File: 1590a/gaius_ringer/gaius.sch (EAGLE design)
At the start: 30 parts, among them Q1 2N5088, Q2 2N3906, Q3 2N5088

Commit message: finished chorus and tremolo baords; other tweaks & polish
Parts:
- removed PAD1: PADSQR, supply pins:PADSQR
- removed PAD3: PADRND, supply pins:PADRND
- added 9V: DC_MONO, jacks:DC_MONO
- C1, C3, C4, C5: device capacitors-film:CER/FILMBOX.1 -> capacitors-film:CER/FILM2
- D1: device diodes:DO41.2 -> diodes:DO41.3
- renumbered PAD2 to IN, PAD4 to GND, PAD5 to OUT
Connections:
- net IN1 renamed IN
- net OUT1 renamed OUT
- removed net +9V: D1.A, PAD1.P$1
- new net N$13: 9V.TIP, D1.A
- net GND: no longer PAD3.P$1
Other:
- note added: "OCTAVER / RING MODULATOR based on the dan armstrong green ringer (c)2016 burr settles"
- note removed: "OCTAVER / RING MODULATOR based on the dan armstrong green ringer (c) 2016 burr settles"
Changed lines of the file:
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@@
 <drawing>
 <settings>
-<setting alwaysvectorfont="no"/>
+<setting alwaysvectorfont="yes"/>
 <setting verticaltext="up"/>
 </settings>
@@
 </classes>
 <parts>
-<part name="C1" library="capacitors-film" deviceset="CER/FILM" device="BOX.1" value="47n"/>
+<part name="C1" library="capacitors-film" deviceset="CER/FILM" device="2" value="47n"/>
 <part name="R3" library="resistors" deviceset="R_" device=".3B" value="160k"/>
 <part name="R2" library="resistors" deviceset="R_" device=".3B" value="470k"/>
@@
 <part name="R7" library="resistors" deviceset="R_" device=".3B" value="10k"/>
 <part name="GND5" library="supply pins" deviceset="GND" device=""/>
-<part name="C3" library="capacitors-film" deviceset="CER/FILM" device="BOX.1" value="47n"/>
+<part name="C3" library="capacitors-film" deviceset="CER/FILM" device="2" value="47n"/>
 <part name="NULL" library="potentiometers" deviceset="POTS" device="TRIM" value="25kB"/>
-<part name="C4" library="capacitors-film" deviceset="CER/FILM" device="BOX.1" value="47n"/>
+<part name="C4" library="capacitors-film" deviceset="CER/FILM" device="2" value="47n"/>
 <part name="R9" library="resistors" deviceset="R_" device=".3B" value="68k"/>
 <part name="R8" library="resistors" deviceset="R_" device=".3B" value="68k"/>
@@
 <part name="R13" library="resistors" deviceset="R_" device=".3B" value="47k"/>
 <part name="GND8" library="supply pins" deviceset="GND" device=""/>
-<part name="D1" library="diodes" deviceset="DO41" device=".2" value="1N5817"/>
+<part name="D1" library="diodes" deviceset="DO41" device=".3" value="1N5817"/>
 <part name="C2" library="capacitors-elec" deviceset="050" device="1" value="100u"/>
 <part name="GND2" library="supply pins" deviceset="GND" device=""/>
-<part name="V1" library="gm-supply" deviceset="+9V" device=""/>
-<part name="IN1" library="gm-supply" deviceset="IN" device=""/>
-<part name="OUT1" library="gm-supply" deviceset="OUT" device=""/>
 <part name="GND1" library="supply pins" deviceset="GND" device=""/>
-<part name="PAD1" library="supply pins" deviceset="PAD" device="SQR"/>
-<part name="PAD2" library="supply pins" deviceset="PAD" device="SQR"/>
-<part name="PAD5" library="supply pins" deviceset="PAD" device="SQR"/>
-<part name="PAD3" library="supply pins" deviceset="PAD" device="RND"/>
-<part name="PAD4" library="supply pins" deviceset="PAD" device="RND"/>
-<part name="C5" library="capacitors-film" deviceset="CER/FILM" device="BOX.1" value="100n"/>
+<part name="IN" library="supply pins" deviceset="PAD" device="SQR"/>
+<part name="OUT" library="supply pins" deviceset="PAD" device="SQR"/>
+<part name="GND" library="supply pins" deviceset="PAD" device="RND"/>
+<part name="C5" library="capacitors-film" deviceset="CER/FILM" device="2" value="100n"/>
+<part name="9V" library="jacks" deviceset="DC_MONO" device=""/>
 </parts>
 <sheets>
@@
 <text x="2.54" y="2.54" size="1.9304" layer="97">OCTAVER / RING MODULATOR
 based on the dan armstrong green ringer
-(c) 2016 burr settles</text>
+(c)2016 burr settles</text>
 </plain>
 <instances>
@@
 <instance part="D1" gate="G$1" x="17.78" y="88.9"/>
 <instance part="C2" gate="1" x="27.94" y="78.74" rot="MR270"/>
-<instance part="GND2" gate="GND" x="27.94" y="66.04"/>
-<instance part="V1" gate="+9V" x="5.08" y="88.9" rot="R90"/>
-<instance part="IN1" gate="G$1" x="5.08" y="48.26"/>
-<instance part="OUT1" gate="G$1" x="132.08" y="43.18"/>
+<instance part="GND2" gate="GND" x="27.94" y="68.58"/>
 <instance part="GND1" gate="GND" x="17.78" y="27.94"/>
-<instance part="PAD1" gate="G$1" x="7.62" y="88.9"/>
-<instance part="PAD2" gate="G$1" x="7.62" y="48.26"/>
-<instance part="PAD5" gate="G$1" x="129.54" y="43.18"/>
-<instance part="PAD3" gate="G$1" x="27.94" y="68.58" rot="R90"/>
-<instance part="PAD4" gate="G$1" x="121.92" y="30.48" rot="R90"/>
+<instance part="IN" gate="G$1" x="7.62" y="48.26"/>
+<instance part="OUT" gate="G$1" x="129.54" y="43.18"/>
+<instance part="GND" gate="G$1" x="121.92" y="30.48" rot="R90"/>
 <instance part="C5" gate="G$1" x="114.3" y="43.18"/>
+<instance part="9V" gate="DC" x="5.08" y="86.36"/>
 </instances>
 <busses>
@@
 <pinref part="R13" gate="G$1" pin="1"/>
 <pinref part="GND8" gate="GND" pin="GND"/>
-<pinref part="PAD4" gate="G$1" pin="P$1"/>
+<pinref part="GND" gate="G$1" pin="P$1"/>
 <junction x="121.92" y="30.48"/>
-<pinref part="PAD4" gate="G$1" pin="P$1"/>
+<pinref part="GND" gate="G$1" pin="P$1"/>
 </segment>
 <segment>
@@
 <pinref part="C2" gate="1" pin="-"/>
 <pinref part="GND2" gate="GND" pin="GND"/>
-<wire x1="27.94" y1="73.66" x2="27.94" y2="68.58" width="0.1524" layer="91"/>
-<pinref part="PAD3" gate="G$1" pin="P$1"/>
-<pinref part="PAD3" gate="G$1" pin="P$1"/>
-<junction x="27.94" y="68.58"/>
+<wire x1="27.94" y1="73.66" x2="27.94" y2="71.12" width="0.1524" layer="91"/>
 </segment>
 </net>
@@
 </segment>
 </net>
-<net name="+9V" class="0">
-<segment>
-<pinref part="V1" gate="+9V" pin="+9V"/>
-<pinref part="PAD1" gate="G$1" pin="P$1"/>
-<pinref part="D1" gate="G$1" pin="A"/>
-<wire x1="12.7" y1="88.9" x2="7.62" y2="88.9" width="0.1524" layer="91"/>
-<junction x="7.62" y="88.9"/>
-</segment>
-</net>
-<net name="IN1" class="0">
+<net name="IN" class="0">
 <segment>
 <wire x1="24.13" y1="48.26" x2="17.78" y2="48.26" width="0.1524" layer="91"/>
@@
 <wire x1="17.78" y1="40.64" x2="17.78" y2="48.26" width="0.1524" layer="91"/>
 <junction x="17.78" y="48.26"/>
-<pinref part="IN1" gate="G$1" pin="IN"/>
-<pinref part="PAD2" gate="G$1" pin="P$1"/>
+<pinref part="IN" gate="G$1" pin="P$1"/>
+<label x="5.08" y="48.26" size="1.778" layer="95" rot="R180" xref="yes"/>
+<wire x1="5.08" y1="48.26" x2="7.62" y2="48.26" width="0.1524" layer="91"/>
 <junction x="7.62" y="48.26"/>
 </segment>
 </net>
-<net name="OUT1" class="0">
+<net name="OUT" class="0">
 <segment>
 <pinref part="R13" gate="G$1" pin="2"/>
@@
 <wire x1="121.92" y1="43.18" x2="121.92" y2="40.64" width="0.1524" layer="91"/>
 <junction x="121.92" y="43.18"/>
-<pinref part="OUT1" gate="G$1" pin="OUT"/>
-<pinref part="PAD5" gate="G$1" pin="P$1"/>
-<junction x="129.54" y="43.18"/>
+<pinref part="OUT" gate="G$1" pin="P$1"/>
 <wire x1="121.92" y1="43.18" x2="118.11" y2="43.18" width="0.1524" layer="91"/>
 <pinref part="C5" gate="G$1" pin="1"/>
+<label x="132.08" y="43.18" size="1.778" layer="95" xref="yes"/>
+<wire x1="132.08" y1="43.18" x2="129.54" y2="43.18" width="0.1524" layer="91"/>
+<junction x="129.54" y="43.18"/>
 </segment>
 </net>
@@
 </segment>
 </net>
+<net name="N$13" class="0">
+<segment>
+<pinref part="D1" gate="G$1" pin="A"/>
+<wire x1="12.7" y1="88.9" x2="10.16" y2="88.9" width="0.1524" layer="91"/>
+<pinref part="9V" gate="DC" pin="TIP"/>
+</segment>
+</net>

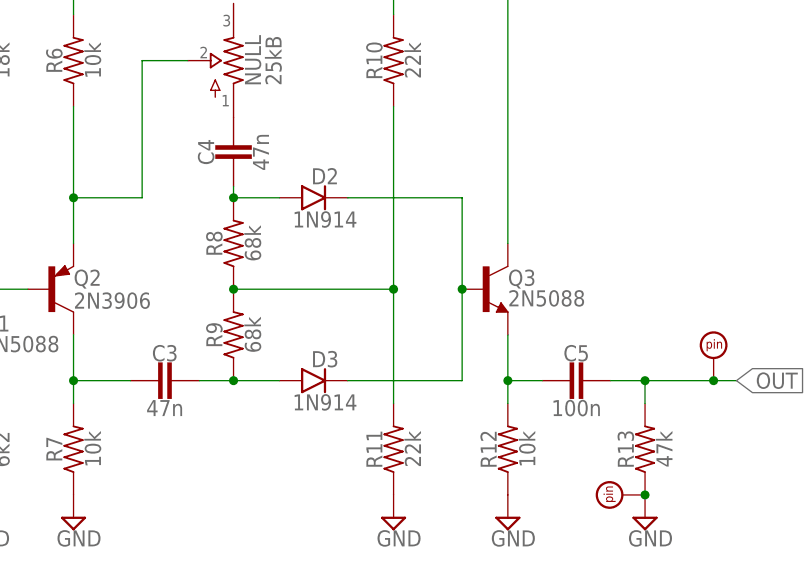
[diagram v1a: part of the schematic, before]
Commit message: prettified schematics a bit
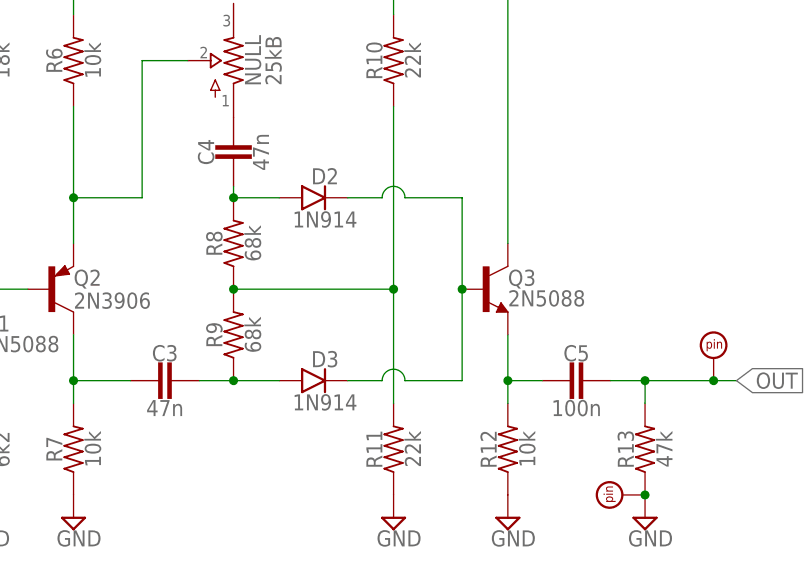
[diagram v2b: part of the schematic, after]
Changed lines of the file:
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@@
 <setting verticaltext="up"/>
 </settings>
-<grid distance="0.1" unitdist="inch" unit="inch" style="lines" multiple="1" display="no" altdistance="0.01" altunitdist="inch" altunit="inch"/>
+<grid distance="0.05" unitdist="inch" unit="inch" style="lines" multiple="2" display="no" altdistance="0.01" altunitdist="inch" altunit="inch"/>
 <layers>
 <layer number="1" name="Top" color="4" fill="1" visible="no" active="no"/>
@@
 <pinref part="D2" gate="G$1" pin="C"/>
 <pinref part="Q3" gate="G$1" pin="B"/>
-<wire x1="88.9" y1="63.5" x2="101.6" y2="63.5" width="0.1524" layer="91"/>
+<wire x1="88.9" y1="63.5" x2="92.71" y2="63.5" width="0.1524" layer="91"/>
+<wire x1="95.25" y1="63.5" x2="101.6" y2="63.5" width="0.1524" layer="91"/>
 <wire x1="101.6" y1="63.5" x2="101.6" y2="53.34" width="0.1524" layer="91"/>
 <pinref part="D3" gate="G$1" pin="C"/>
-<wire x1="88.9" y1="43.18" x2="101.6" y2="43.18" width="0.1524" layer="91"/>
+<wire x1="88.9" y1="43.18" x2="92.71" y2="43.18" width="0.1524" layer="91"/>
+<wire x1="95.25" y1="43.18" x2="101.6" y2="43.18" width="0.1524" layer="91"/>
 <wire x1="101.6" y1="43.18" x2="101.6" y2="53.34" width="0.1524" layer="91"/>
 <junction x="101.6" y="53.34"/>
-</segment>
-</net>
+<wire x1="92.71" y1="63.5" x2="95.25" y2="63.5" width="0.1524" layer="91" curve="-180" cap="flat"/>
+<wire x1="92.71" y1="43.18" x2="95.25" y2="43.18" width="0.1524" layer="91" curve="-180" cap="flat"/>
+</segment>
+</net>

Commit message: added RT logo; converted some pots trimmers
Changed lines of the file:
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@@
 <setting verticaltext="up"/>
 </settings>
-<grid distance="0.05" unitdist="inch" unit="inch" style="lines" multiple="2" display="no" altdistance="0.01" altunitdist="inch" altunit="inch"/>
+<grid distance="0.1" unitdist="inch" unit="inch" style="lines" multiple="1" display="no" altdistance="0.01" altunitdist="inch" altunit="inch"/>
 <layers>
 <layer number="1" name="Top" color="4" fill="1" visible="no" active="no"/>
@@
 <part name="C5" library="capacitors-film" deviceset="CER/FILM" device="2" value="100n"/>
 <part name="9V" library="jacks" deviceset="DC_MONO" device=""/>
+<part name="U$2" library="logos" deviceset="REBELSTRUST" device=""/>
 </parts>
 <sheets>
@@
 <instance part="C5" gate="G$1" x="114.3" y="43.18"/>
 <instance part="9V" gate="DC" x="5.08" y="86.36"/>
+<instance part="U$2" gate="G$1" x="71.12" y="2.54"/>
 </instances>
 <busses>

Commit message: little edits & cleanup
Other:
- note added: "GAIUS"
- note removed: "GAIUS RINGER"
- moved on the sheet: 9V, C1, C2, C3, C4, C5, D1, D2, D3, NULL, Q1, Q2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

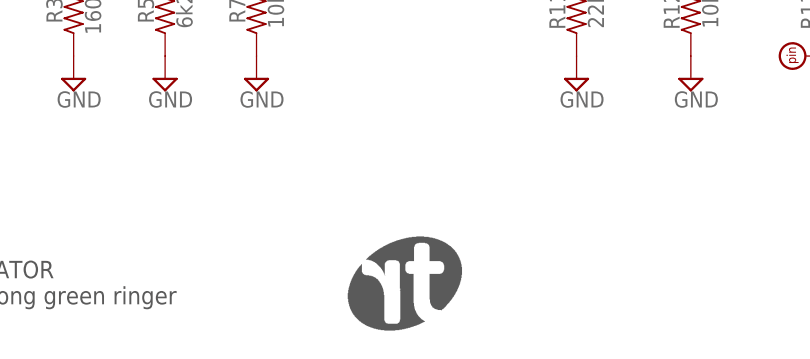
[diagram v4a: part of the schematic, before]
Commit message: convert bitmap logos to polygons
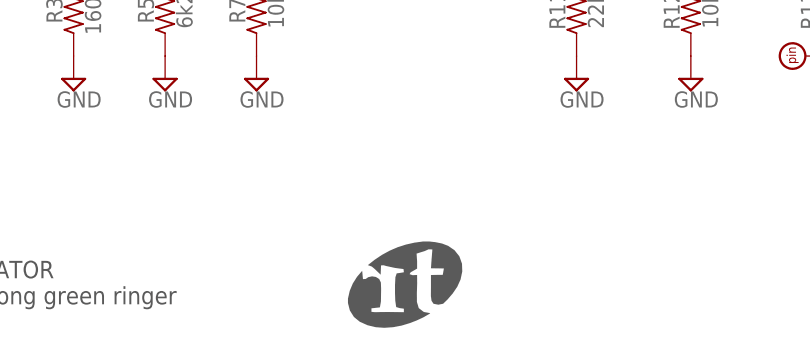
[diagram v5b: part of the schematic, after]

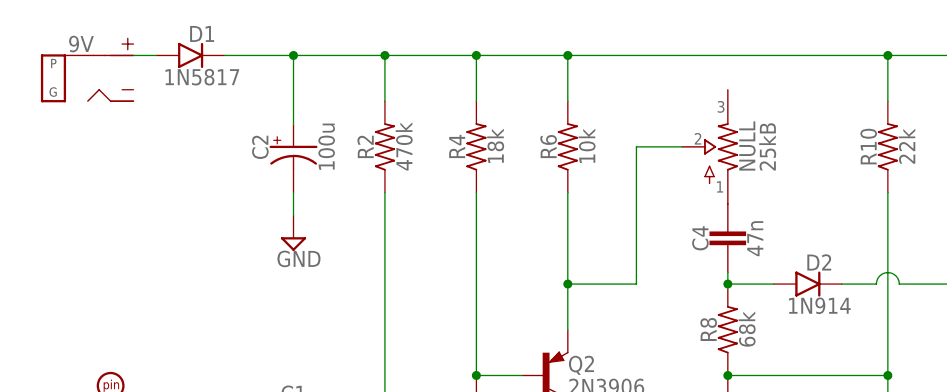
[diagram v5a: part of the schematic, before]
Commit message: add GAIUS documentation
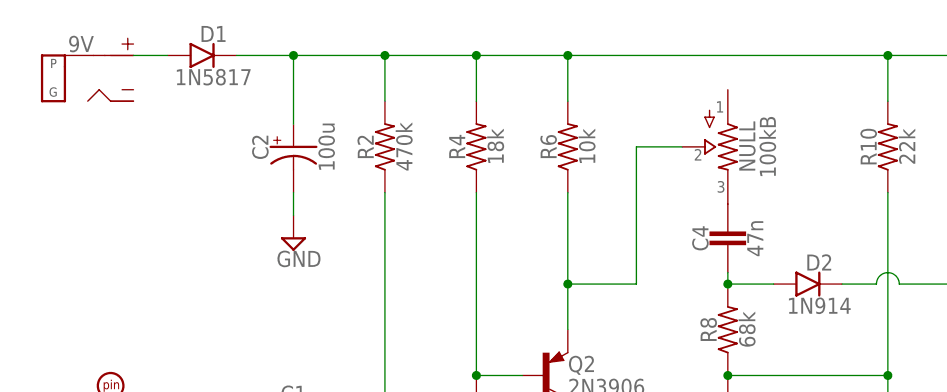
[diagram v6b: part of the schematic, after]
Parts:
- NULL: value 25kB -> 100kB
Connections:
- net N$7: now also NULL.3; no longer NULL.1
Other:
- moved on the sheet: D1, NULL
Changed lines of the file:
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@@
 <setting verticaltext="up"/>
 </settings>
-<grid distance="0.1" unitdist="inch" unit="inch" style="lines" multiple="1" display="no" altdistance="0.01" altunitdist="inch" altunit="inch"/>
+<grid distance="0.05" unitdist="inch" unit="inch" style="lines" multiple="2" display="no" altdistance="0.01" altunitdist="inch" altunit="inch"/>
 <layers>
 <layer number="1" name="Top" color="4" fill="1" visible="no" active="no"/>
@@
 <part name="GND5" library="supply pins" deviceset="GND" device=""/>
 <part name="C3" library="capacitors-film" deviceset="CER/FILM" device="2" value="47n"/>
-<part name="NULL" library="potentiometers" deviceset="POTS" device="TRIM" value="25kB"/>
+<part name="NULL" library="potentiometers" deviceset="POTS" device="TRIM" value="100kB"/>
 <part name="C4" library="capacitors-film" deviceset="CER/FILM" device="2" value="47n"/>
 <part name="R9" library="resistors" deviceset="R_" device=".3B" value="68k"/>
@@
 <instance part="GND5" gate="GND" x="60.96" y="30.48"/>
 <instance part="C3" gate="G$1" x="71.12" y="45.72"/>
-<instance part="NULL" gate="G$1" x="78.74" y="81.28" rot="MR0"/>
+<instance part="NULL" gate="G$1" x="78.74" y="81.28" rot="R180"/>
 <instance part="C4" gate="G$1" x="78.74" y="71.12" rot="R90"/>
 <instance part="R9" gate="G$1" x="78.74" y="50.8" rot="R90"/>
@@
 <instance part="R13" gate="G$1" x="124.46" y="38.1" rot="R90"/>
 <instance part="GND8" gate="GND" x="124.46" y="30.48"/>
-<instance part="D1" gate="G$1" x="20.32" y="91.44"/>
+<instance part="D1" gate="G$1" x="21.59" y="91.44"/>
 <instance part="C2" gate="1" x="30.48" y="81.28" rot="MR270"/>
 <instance part="GND2" gate="GND" x="30.48" y="71.12"/>
@@
 <wire x1="96.52" y1="76.2" x2="96.52" y2="55.88" width="0.1524" layer="91"/>
 <junction x="96.52" y="55.88"/>
-</segment>
-</net>
-<net name="N$7" class="0">
-<segment>
-<pinref part="C4" gate="G$1" pin="1"/>
-<pinref part="NULL" gate="G$1" pin="1"/>
 </segment>
 </net>
@@
 <junction x="96.52" y="91.44"/>
 <pinref part="D1" gate="G$1" pin="C"/>
-<wire x1="22.86" y1="91.44" x2="30.48" y2="91.44" width="0.1524" layer="91"/>
+<wire x1="24.13" y1="91.44" x2="30.48" y2="91.44" width="0.1524" layer="91"/>
 <junction x="30.48" y="91.44"/>
 </segment>
@@
 <segment>
 <pinref part="D1" gate="G$1" pin="A"/>
-<wire x1="15.24" y1="91.44" x2="12.7" y2="91.44" width="0.1524" layer="91"/>
+<wire x1="16.51" y1="91.44" x2="12.7" y2="91.44" width="0.1524" layer="91"/>
 <pinref part="9V" gate="DC" pin="TIP"/>
 </segment>
 </net>
+<net name="N$7" class="0">
+<segment>
+<pinref part="C4" gate="G$1" pin="1"/>
+<pinref part="NULL" gate="G$1" pin="3"/>
+</segment>
+</net>

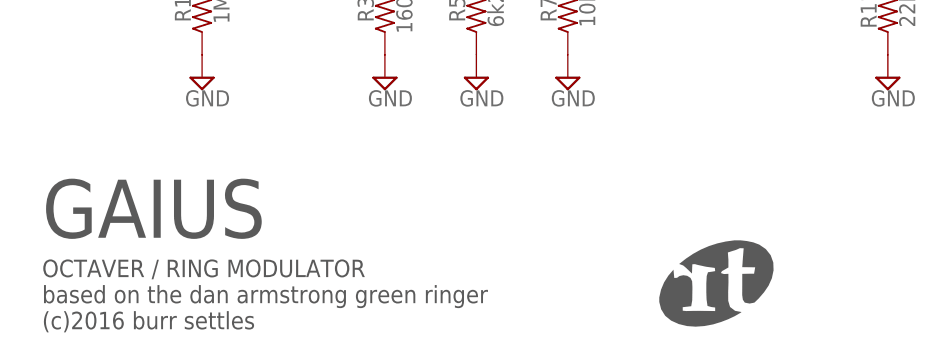
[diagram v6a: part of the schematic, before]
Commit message: updated library + logos
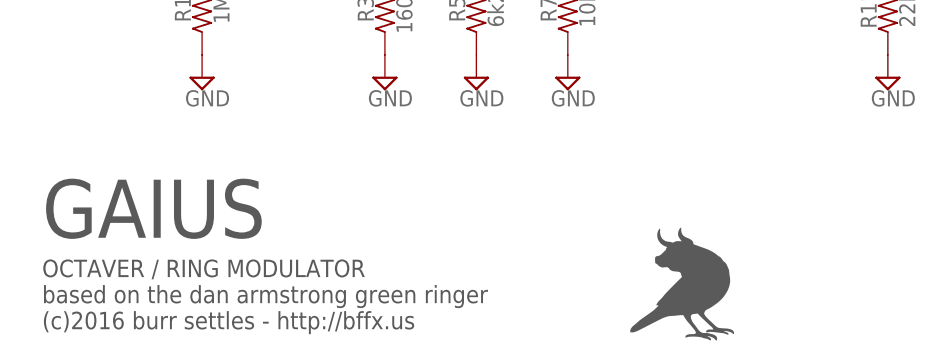
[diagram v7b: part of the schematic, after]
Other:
- note added: "OCTAVER / RING MODULATOR based on the dan armstrong green ringer (c)2016 burr settles - http://bffx.us"
- note removed: "OCTAVER / RING MODULATOR based on the dan armstrong green ringer (c)2016 burr settles"
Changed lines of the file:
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@@
 <setting verticaltext="up"/>
 </settings>
-<grid distance="0.05" unitdist="inch" unit="inch" style="lines" multiple="2" display="no" altdistance="0.01" altunitdist="inch" altunit="inch"/>
+<grid distance="0.1" unitdist="inch" unit="inch" style="lines" multiple="1" display="no" altdistance="0.01" altunitdist="inch" altunit="inch"/>
 <layers>
 <layer number="1" name="Top" color="4" fill="1" visible="no" active="no"/>
@@
 <part name="C5" library="capacitors-film" deviceset="CER/FILM" device="2" value="100n"/>
 <part name="9V" library="jacks" deviceset="DC_MONO" device=""/>
-<part name="U$2" library="logos" deviceset="REBELSTRUST" device=""/>
+<part name="BF1" library="logos" deviceset="BULLFINCH" device=""/>
 </parts>
 <sheets>
@@
 <text x="2.54" y="2.54" size="1.9304" layer="97">OCTAVER / RING MODULATOR
 based on the dan armstrong green ringer
-(c)2016 burr settles</text>
+(c)2016 burr settles - http://bffx.us</text>
 </plain>
 <instances>
@@
 <instance part="C5" gate="G$1" x="116.84" y="45.72"/>
 <instance part="9V" gate="DC" x="7.62" y="88.9"/>
-<instance part="U$2" gate="G$1" x="71.12" y="2.54"/>
+<instance part="BF1" gate="G$1" x="73.66" y="7.62"/>
 </instances>
 <busses>
